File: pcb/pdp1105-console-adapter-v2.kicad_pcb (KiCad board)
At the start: 2 copper layers, 73 x 34 mm, 23 parts, among them J1 SCL Connector, J2 DE9_Plug, Q1 MMBT3904, U1 Pico, U2 MAX3232

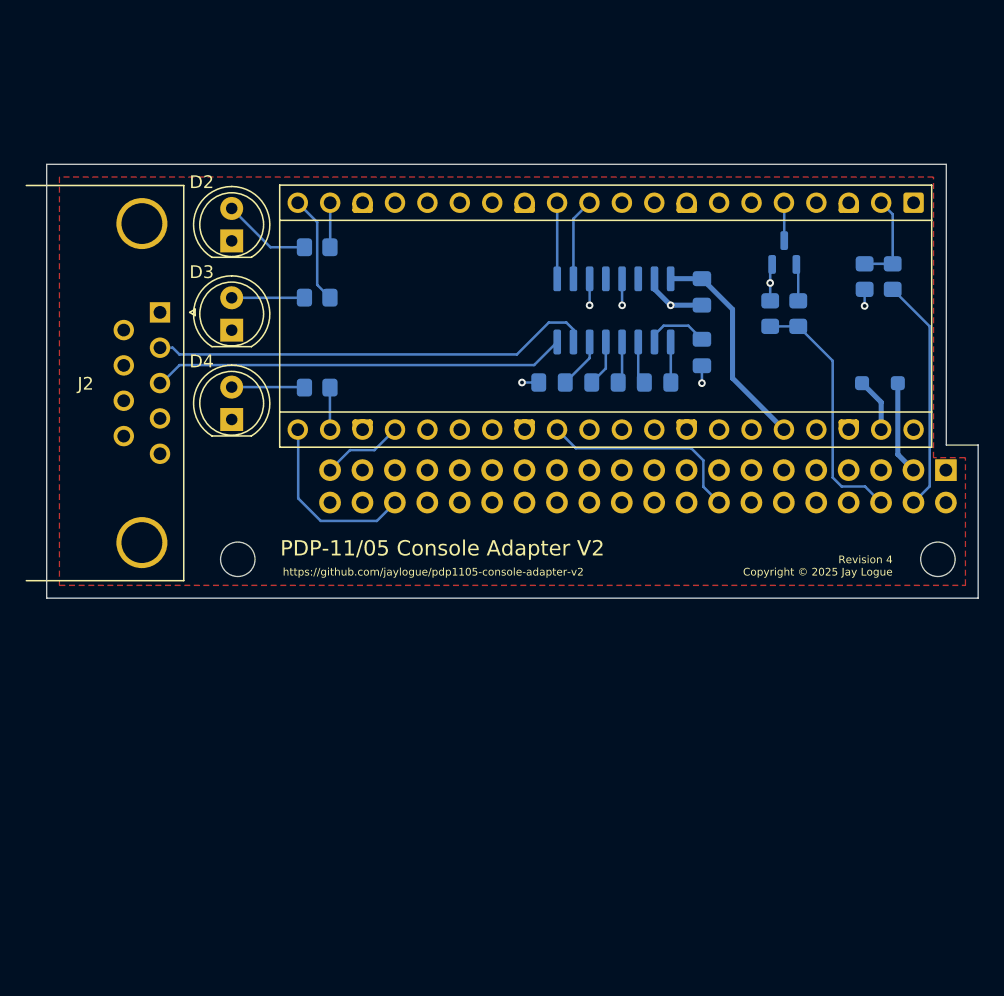
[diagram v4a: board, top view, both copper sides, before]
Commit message: Revision 4.1 Schematic and PCB Design
-- Switch to female DE9 connector for Aux port.

-- Added solder jumpers to select between DTE and DCE configuration for Aux
port. Default is set to DCE.

-- Revised LED component layout to allow for copper keep-out area under
Pico W antenna.

-- Added copper ground fill on PCB backside.

-- Cleaned up copper fill on frontside.

-- Made various silkscreen additions to identify part names and orientations.

-- Added PCB layer PDF.

-- Added PCB 3d renderings.
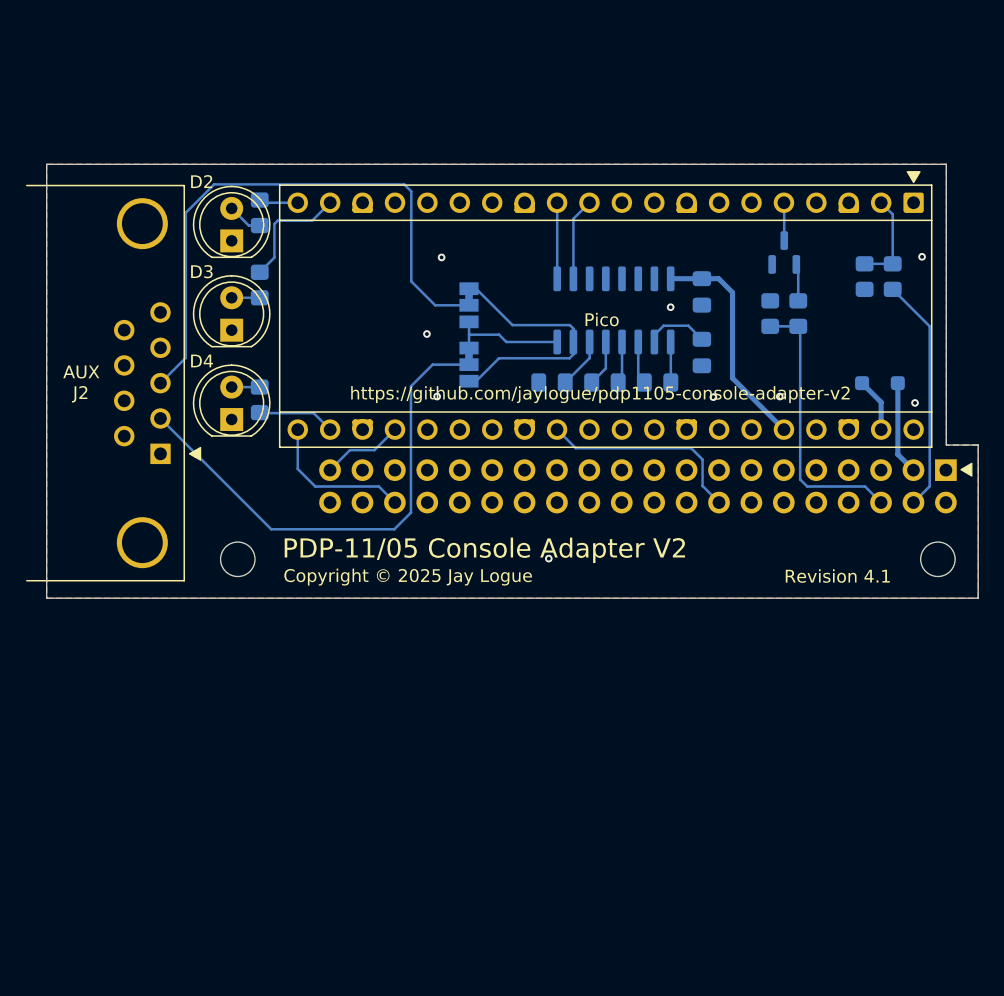
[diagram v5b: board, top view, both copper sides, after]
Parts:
- added JP1: SolderJumper_3_Bridged12, Jumper:SolderJumper-3_P1.3mm_Bridged12_Pad1.0x1.5mm, B.Cu at (138.3, 86.6)
- added JP2: SolderJumper_3_Bridged12, Jumper:SolderJumper-3_P1.3mm_Bridged12_Pad1.0x1.5mm, B.Cu at (138.3, 91.2)
- J1: value SCL Connector -> PDP-11/05 SCL
- J2: value DE9_Plug -> AUX; footprint Connector_Dsub:DSUB-9_Male_Horizontal_P2.77x2.84mm_EdgePinOffset7.70mm_Housed_MountingHolesOffset9.12mm -> Connector_Dsub:DSUB-9_Female_Horizontal_P2.77x2.84mm_EdgePinOffset7.70mm_Housed_MountingHolesOffset9.12mm
- moved J2 11.1 mm to (114.1, 98.2)
- moved R5 5.25 mm to (121.9, 79.3), turned to -90 degrees
- moved R6 4.61 mm to (121.9, 85.0), turned to -90 degrees
- moved R7 4.60 mm to (121.9, 94.0), turned to 90 degrees
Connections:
- J2 pad 2: Net-(U2-T2OUT) -> Net-(JP2-C)
- J2 pad 3: Net-(U2-R2IN) -> Net-(JP1-C)
- U1 pad 19: STATUS_LED -> TX_LED
- U1 pad 20: TX_LED -> STATUS_LED
- U2 pad 7: Net-(U2-T2OUT) -> Net-(JP1-A)
- U2 pad 8: Net-(U2-R2IN) -> Net-(JP1-B)
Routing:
- net Net-(JP1-C): track 0.00 -> 45.5 mm
- net Net-(JP2-C): track 0.00 -> 38.9 mm
- net Net-(U2-T2OUT): track 34.9 -> 0.00 mm
- net Net-(U2-R2IN): track 32.5 -> 0.00 mm
- net Net-(JP1-A): track 0.00 -> 20.5 mm
- net GND: track 16.1 -> 0.21 mm, vias 7 -> 9
- net Net-(JP1-B): track 0.00 -> 9.20 mm
- net Net-(D2-A): track 6.96 -> 2.76 mm
- net Net-(D4-A): track 5.72 -> 2.20 mm
- net Net-(D3-A): track 5.70 -> 2.20 mm
- net SERIAL_IN_TTL: track 14.3 -> 11.8 mm
- net RX_LED: track 3.30 -> 5.75 mm
- net READER_RUN+: track 19.8 -> 21.3 mm
- net TX_LED: track 8.48 -> 9.32 mm
- net +3V3: track 16.9 -> 17.7 mm
- added copper zone on B.Cu, net GND
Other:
- board text added: "AUX"
- board text added: "AUX J2"
- board text added: "Copyright © 2025 Jay Logue"
- board text added: "DCE"
- board text added: "DTE"
- board text added: "PDP-11/05 SCL"
- board text added: "Pico"
- board text added: "Revision 4.1"
- board text removed: "Revision 4 Copyright © 2025 Jay Logue"

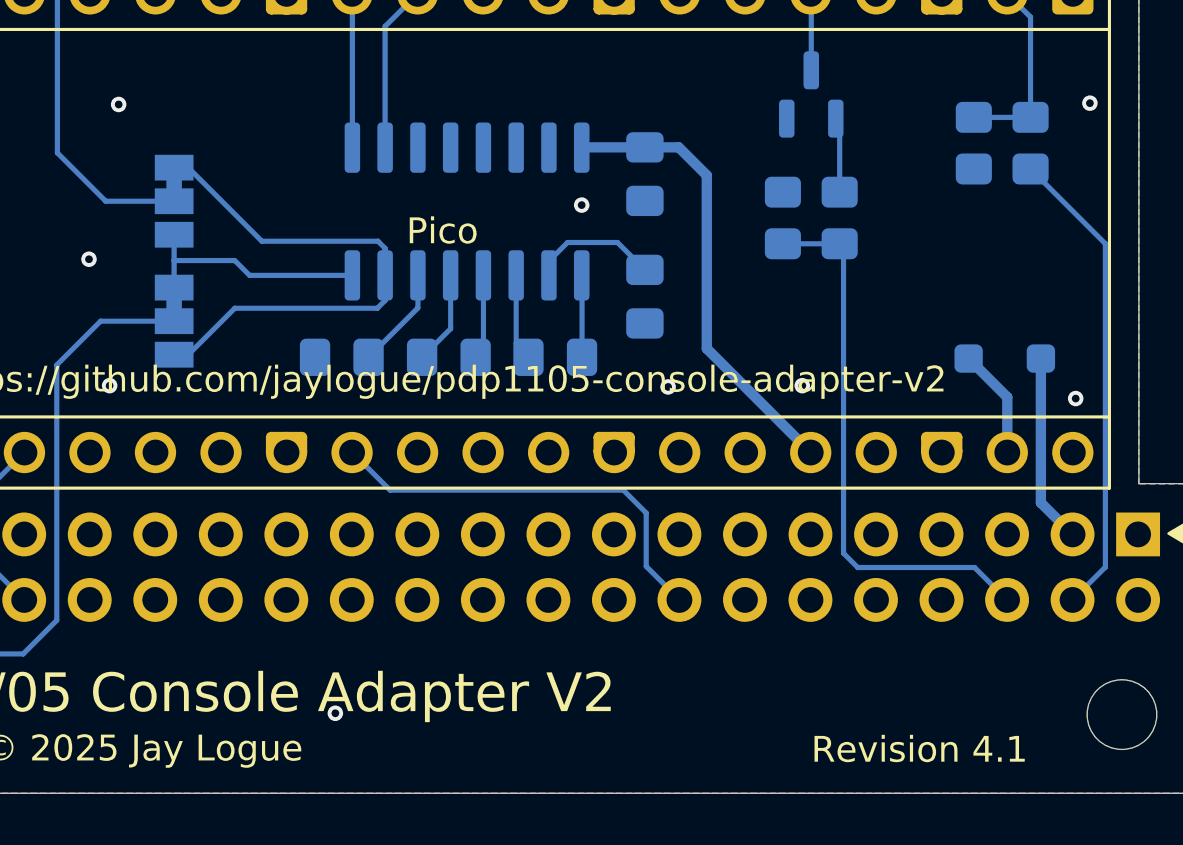
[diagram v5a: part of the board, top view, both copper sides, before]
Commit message: ﻿Revision 4.2 Schematic and PCB Design
-- Fixed bug in schematic that resulted in the AUX port defaulting to DTE
configuration instead of DCE.

-- Fixed bug in PCB silkscreen that mislabeled the jumper configuration for
choosing AUX port DTE vs. DCE configuration.

Note that revision 4.2 is firmware compatible with revision 4.1.
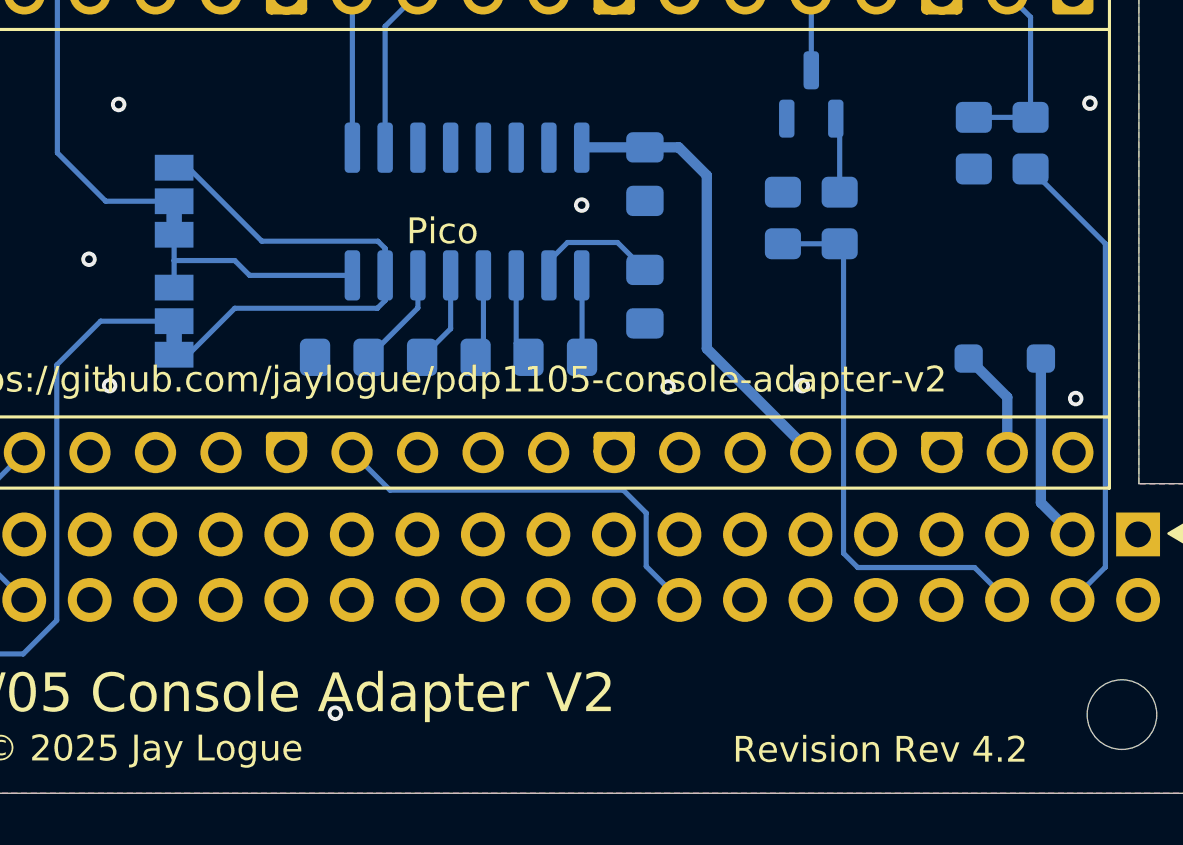
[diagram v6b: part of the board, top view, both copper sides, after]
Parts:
- turned JP1 to 90 degrees
- turned JP2 to 90 degrees
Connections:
- J1 pad 24: unconnected-(J1--15V-Pad24) -> -15V
- U2 pad 7: Net-(JP1-A) -> Net-(JP1-B)
- U2 pad 8: Net-(JP1-B) -> Net-(JP1-A)
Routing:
- net Net-(JP1-B): track 9.20 -> 20.5 mm
- net Net-(JP1-A): track 20.5 -> 9.20 mm
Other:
- board text added: "${COMMENT2}"
- board text added: "${COMMENT4}"
- board text added: "${TITLE}"
- board text added: "Revision ${REVISION}"
- board text removed: "AUX J2"
- board text removed: "Copyright © 2025 Jay Logue"
- board text removed: "PDP-11/05 Console Adapter V2"
- board text removed: "Revision 4.1"
- board text removed: "https://github.com/jaylogue/pdp1105-console-adapter-v2"
